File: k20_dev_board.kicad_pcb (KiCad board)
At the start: 4 copper layers, 53.3 x 81.3 mm, 52 parts, among them J1 USB_OTG, J2 MIDI-DIN-5, J3 Conn_02x10_Odd_Even, J4 Conn_02x10_Odd_Even, J5 Conn_02x08_Odd_Even, J6 Conn_02x08_Odd_Even, J7 Conn_02x06_Odd_Even, SW1 SW_Push, U1 H11L1, U2 MCP1702T-3302E/CB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

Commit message: Reordered breakout pins to be manageable
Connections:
- J4 pad 1: /PTB16 -> Net-(J4-Pad1)
- J4 pad 10: /PTD3 -> /PTD6/FTM0_CH6
- J4 pad 12: /PTD1 -> /PTD7/FTM0_CH7
- J4 pad 13: Net-(J4-Pad13) -> /PTE0/UART1_TX
- J4 pad 15: Net-(J4-Pad15) -> /PTE1/UART1_RX
- J4 pad 17: Net-(J4-Pad17) -> /ADC0_DM0
- J4 pad 18: /PTB3 -> /ADC0_DP0
- J4 pad 19: Net-(J4-Pad19) -> /ADC0_DM3
- J4 pad 20: /PTB2 -> /ADC0_DP3
- J4 pad 3: /PTB17 -> Net-(J4-Pad3)
- J4 pad 4: /PTA12/FTM1_CH0 -> /PTD3
- J4 pad 5: /PTB18 -> Net-(J4-Pad5)
- J4 pad 6: /PTA13/FTM1_CH1 -> /PTD4/FTM0_CH4
- J4 pad 8: /PTD7/FTM0_CH7 -> /PTD5/FTM0_CH5
- J5 pad 1: /PTD0 -> /PTB18
- J5 pad 10: /PTC8 -> /PTC7
- J5 pad 11: /PTA4 -> /PTC8
- J5 pad 12: /PTC2/FTM0_CH1 -> /PTC9
- J5 pad 13: /PTB19 -> /PTC10
- J5 pad 14: /PTC3/FTM0_CH2 -> /PTC11
- J5 pad 15: /PTC9 -> /PTD0
- J5 pad 16: /PTC4/FTM0_CH3 -> /PTD1
- J5 pad 2: /PTE1/UART1_RX -> /PTB19
- J5 pad 3: /PTC11 -> /PTC0
- J5 pad 4: /PTE0/UART1_TX -> /PTC1/FTM0_CH0
- J5 pad 5: /PTC5 -> /PTC2/FTM0_CH1
- J5 pad 6: /PTC10 -> /PTC3/FTM0_CH2
- J5 pad 7: /PTC6 -> /PTC4/FTM0_CH3
- J5 pad 8: /PTD4/FTM0_CH4 -> /PTC5
- J5 pad 9: /PTC7 -> /PTC6
- J7 pad 1: /CMP1_IN5 -> /PTA13/FTM1_CH1
- J7 pad 10: /PTB1/FTM1_CH1 -> /PTB16
- J7 pad 11: /ADC0_DM0 -> Net-(J7-Pad11)
- J7 pad 12: /PTB0/FTM1_CH0 -> /PTB17
- J7 pad 2: /PTC0 -> /PTA12/FTM1_CH0
- J7 pad 3: /CMP1_IN3 -> /PTB1/FTM1_CH1
- J7 pad 4: /PTC1/FTM0_CH0 -> /PTB0/FTM1_CH0
- J7 pad 5: /ADC0_DP3 -> Net-(J7-Pad5)
- J7 pad 6: /PTD6/FTM0_CH6 -> /PTB2
- J7 pad 7: /ADC0_DM3 -> Net-(J7-Pad7)
- J7 pad 8: /PTD5/FTM0_CH5 -> /PTB3
- J7 pad 9: /ADC0_DP0 -> Net-(J7-Pad9)
- U3 pad 17: /CMP1_IN5 -> Net-(U3-Pad17)
- U3 pad 18: /CMP1_IN3 -> Net-(U3-Pad18)
- U3 pad 26: /PTA4 -> Net-(U3-Pad26)
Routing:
- net /CMP1_IN3: track 54.1 -> 0.00 mm, vias 2 -> 0
- net /CMP1_IN5: track 50.5 -> 0.00 mm, vias 2 -> 0
- net /PTB1/FTM1_CH1: track 0.00 -> 41.4 mm, vias 0 -> 1
- net /PTA13/FTM1_CH1: track 0.00 -> 40.1 mm, vias 0 -> 1
- net Net-(U3-Pad18): track 0.00 -> 12.8 mm, vias 0 -> 1
- net Net-(U3-Pad17): track 0.00 -> 10.3 mm, vias 0 -> 1

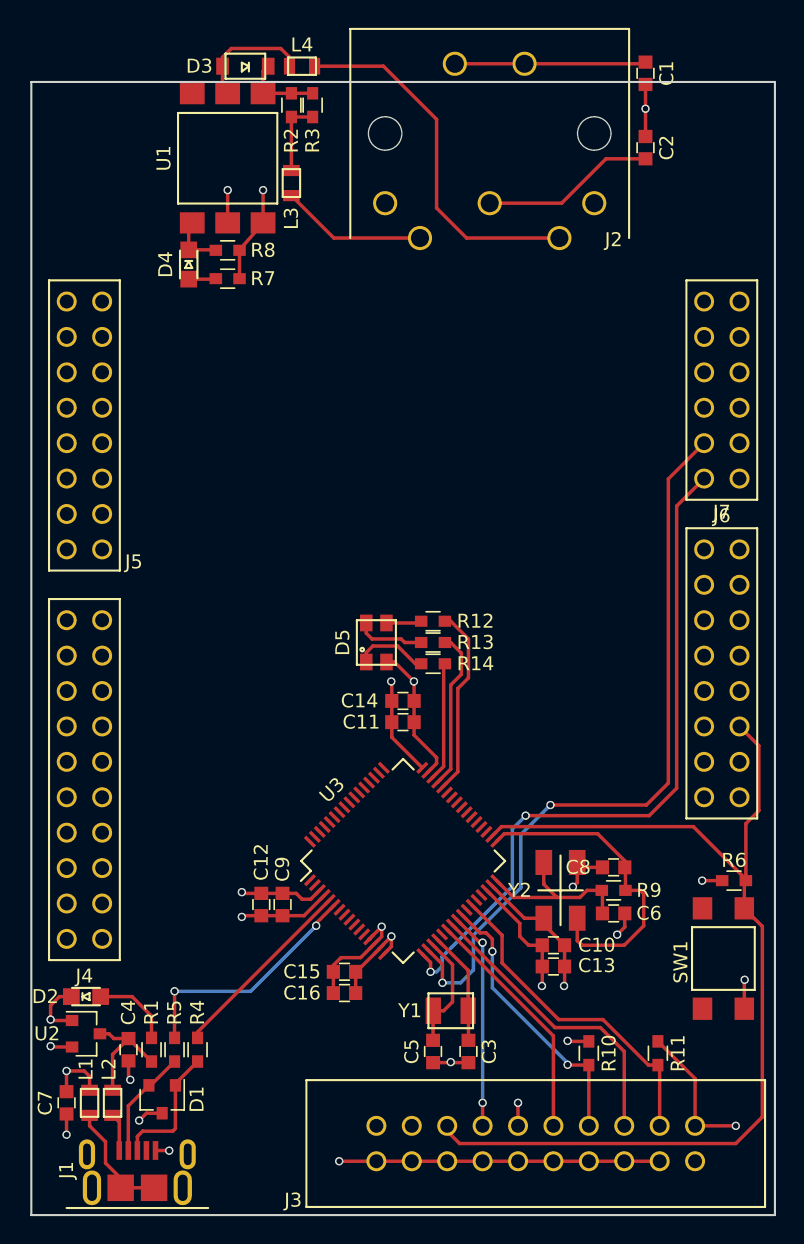
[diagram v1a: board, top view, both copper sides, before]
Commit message: Finished adding traces to layout
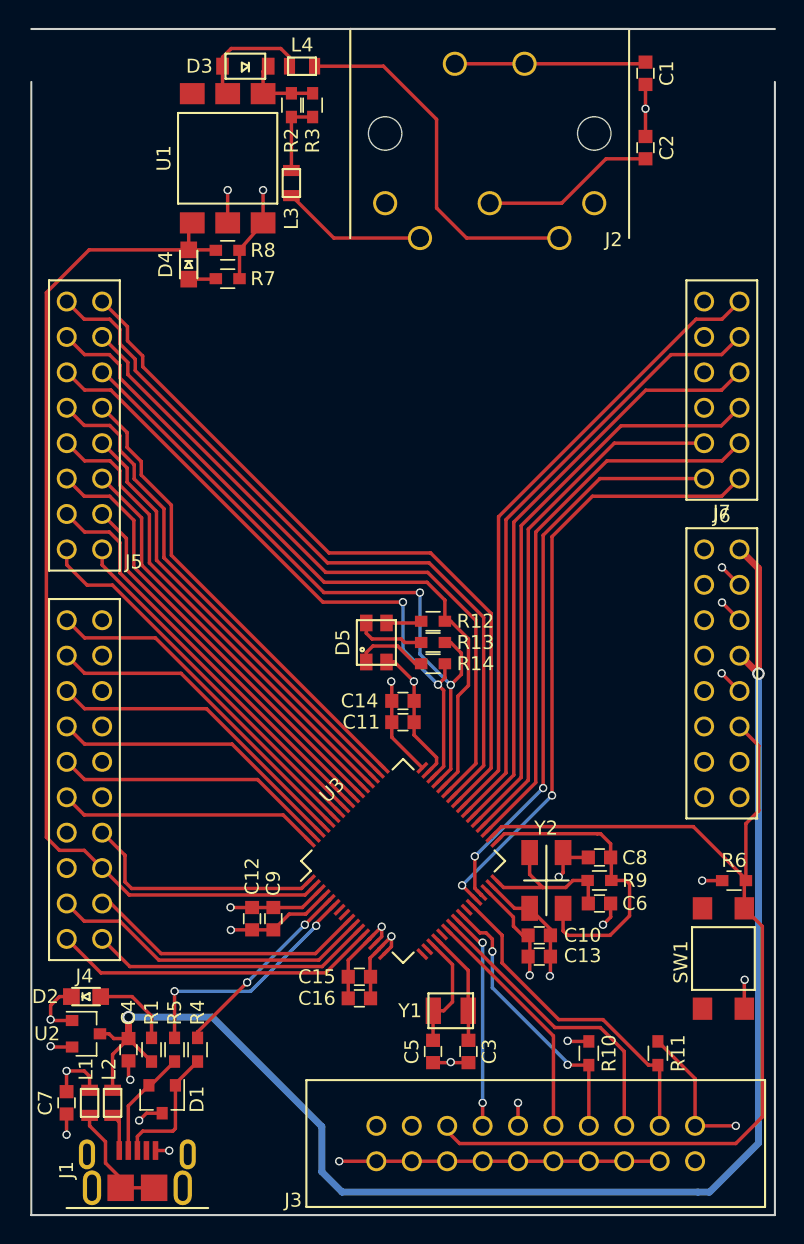
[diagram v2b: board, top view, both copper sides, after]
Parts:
- moved C10 1.24 mm to (159.8, 120.6)
- moved C13 1.24 mm to (159.8, 122.1)
- moved C8 1.24 mm to (164.1, 115.0)
- moved R9 1.24 mm to (164.1, 116.6)
- moved Y2 1.24 mm to (160.3, 116.6)
- moved C6 1.24 mm to (164.1, 118.3)
- moved C12 1.21 mm to (139.2, 119.4)
- moved C9 1.21 mm to (140.7, 119.4)
- moved C16 1.13 mm to (146.9, 125.1)
- moved C15 1.12 mm to (146.9, 123.5)
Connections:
- J4 pad 17: /ADC0_DM0 -> /ADC0_DP0
- J4 pad 18: /ADC0_DP0 -> /ADC0_DM0
- J4 pad 19: /ADC0_DM3 -> /ADC0_DP3
- J4 pad 20: /ADC0_DP3 -> /ADC0_DM3
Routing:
- net +5V: track 8.71 -> 109.0 mm, vias 0 -> 2
- net /PTE1/UART1_RX: track 4.02 -> 75.8 mm
- net /PTB19: track 0.00 -> 54.2 mm
- net /PTB18: track 0.00 -> 52.8 mm
- net /PTC0: track 0.00 -> 48.9 mm
- net /PTB17: track 0.00 -> 45.6 mm
- net /PTA12/FTM1_CH0: track 0.00 -> 44.3 mm, vias 0 -> 2
- net /PTB16: track 0.00 -> 44.3 mm
- net /PTB3: track 0.00 -> 43.1 mm
- net /PTB2: track 0.00 -> 41.7 mm
- net /PTB0/FTM1_CH0: track 0.00 -> 40.2 mm
- net /PTC3/FTM0_CH2: track 8.57 -> 46.9 mm, vias 0 -> 2
- net /PTC1/FTM0_CH0: track 13.7 -> 50.7 mm
- net /PTC2/FTM0_CH1: track 11.5 -> 48.4 mm, vias 0 -> 2
- net /PTC5: track 0.00 -> 36.5 mm
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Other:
- board size 53.3 x 81.3 mm -> 53.3 x 85.1 mm
- net class Power added: clearance 0.5, trace_width 0.5, via_dia 0.9, via_drill 0.6

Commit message: extended copper fills to match larger board size
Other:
- outline, holes or cut-outs redrawn
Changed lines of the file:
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@@
-(kicad_pcb (version 4) (host pcbnew 4.0.7)
+(kicad_pcb (version 4) (host pcbnew 4.0.7-e2-6376~58~ubuntu16.04.1)
   (general
     (links 160)
-    (no_connects 1)
-    (area 123.254999 59.284999 176.745001 140.715001)
+    (no_connects 0)
+    (area 118.396857 54.980499 177.791 140.948)
     (thickness 1.6)
     (drawings 4)
@@
     (tags "capacitor 0603")
     (attr smd)
-    (fp_text reference C4 (at 2.667 0 90) (layer F.SilkS)
+    (fp_text reference C4 (at 3.937 0 90) (layer F.SilkS)
       (effects (font (size 1 1) (thickness 0.15)))
     )
@@
   (module k20_dev_board:PPTC102LFBN-RC (layer F.Cu)
     (at 127.14 109.4)
-    (fp_text reference J4 (at 0 14.097) (layer F.SilkS)
+    (fp_text reference J4 (at -0.013 -13.769) (layer F.SilkS)
       (effects (font (size 1 1) (thickness 0.15)))
     )
@@
   (module k20_dev_board:PPTC082LFBN-RC (layer F.Cu)
     (at 127.14 84)
-    (fp_text reference J5 (at 3.543 9.788) (layer F.SilkS)
+    (fp_text reference J5 (at -0.013 -11.229) (layer F.SilkS)
       (effects (font (size 1 1) (thickness 0.15)))
     )
@@
   (module k20_dev_board:PPTC062LFBN-RC (layer F.Cu)
     (at 172.86 81.46)
-    (fp_text reference J7 (at 0 8.763) (layer F.SilkS)
+    (fp_text reference J7 (at -0.013 -8.689) (layer F.SilkS)
       (effects (font (size 1 1) (thickness 0.15)))
     )
@@
   (module k20_dev_board:PPTC082LFBN-RC (layer F.Cu)
     (at 172.86 101.78 180)
-    (fp_text reference J6 (at 0 11.303 180) (layer F.SilkS)
+    (fp_text reference J6 (at 0.013 11.229 180) (layer F.SilkS)
       (effects (font (size 1 1) (thickness 0.15)))
     )
@@
   )
   (gr_line (start 123.33 55.56) (end 176.67 55.56) (angle 90) (layer Edge.Cuts) (width 0.15))
-  (gr_line (start 176.67 59.36) (end 176.67 140.64) (angle 90) (layer Edge.Cuts) (width 0.15))
+  (gr_line (start 176.67 55.56) (end 176.67 140.64) (angle 90) (layer Edge.Cuts) (width 0.15))
   (gr_line (start 123.33 140.64) (end 176.67 140.64) (angle 90) (layer Edge.Cuts) (width 0.15))
-  (gr_line (start 123.33 140.64) (end 123.33 59.36) (angle 90) (layer Edge.Cuts) (width 0.15))
+  (gr_line (start 123.33 140.64) (end 123.33 55.56) (angle 90) (layer Edge.Cuts) (width 0.15))
   (segment (start 164.884 119.2276) (end 164.884 119.2658) (width 0.25) (layer F.Cu) (net 1))
   (segment (start 164.884 119.2658) (end 164.338 119.8118) (width 0.25) (layer F.Cu) (net 1))
@@
     (polygon
       (pts
-        (xy 123.317 59.309) (xy 123.317 140.589) (xy 176.657 140.589) (xy 176.657 59.309)
+        (xy 123.317 55.626) (xy 123.317 140.589) (xy 176.657 140.589) (xy 176.657 55.626)
       )
     )
@@
     (polygon
       (pts
-        (xy 123.317 59.309) (xy 123.317 140.589) (xy 176.657 140.589) (xy 176.657 59.309)
+        (xy 123.317 55.626) (xy 123.317 140.589) (xy 176.657 140.589) (xy 176.657 55.626)
       )
     )
